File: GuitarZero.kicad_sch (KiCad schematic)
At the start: 9 parts, among them J2 USB_B_Micro, J3 AudioJack3_SwitchT, SW1 SW_Push, SW2 SW_Push, SW3 SW_Push, SW4 SW_Push, SW5 SW_Push, SW6 SW_Push

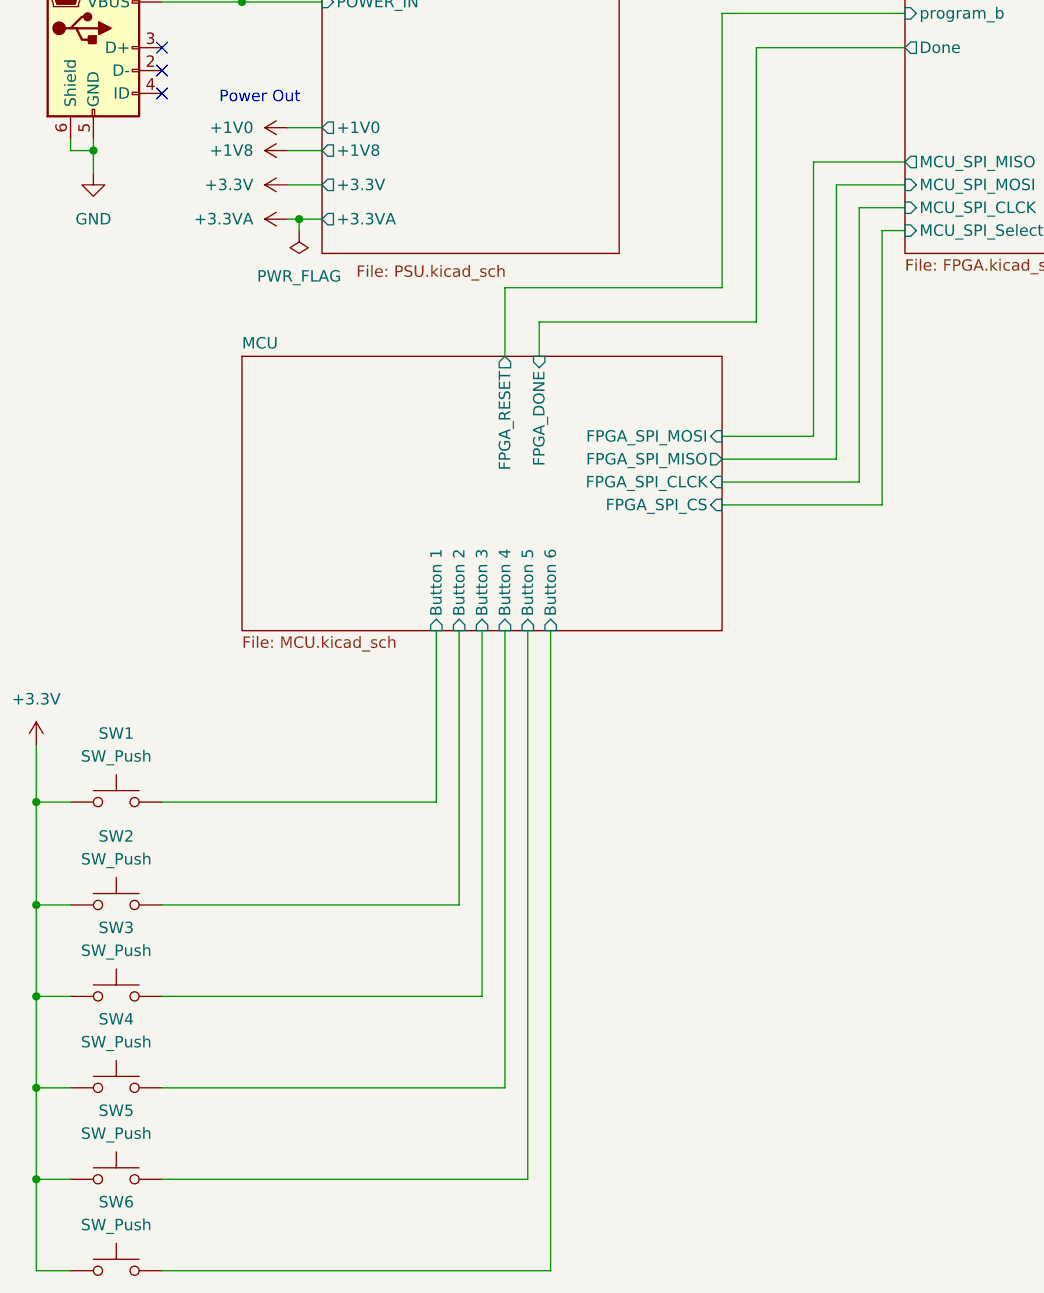
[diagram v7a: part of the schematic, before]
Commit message: Added labels in root for USB signals
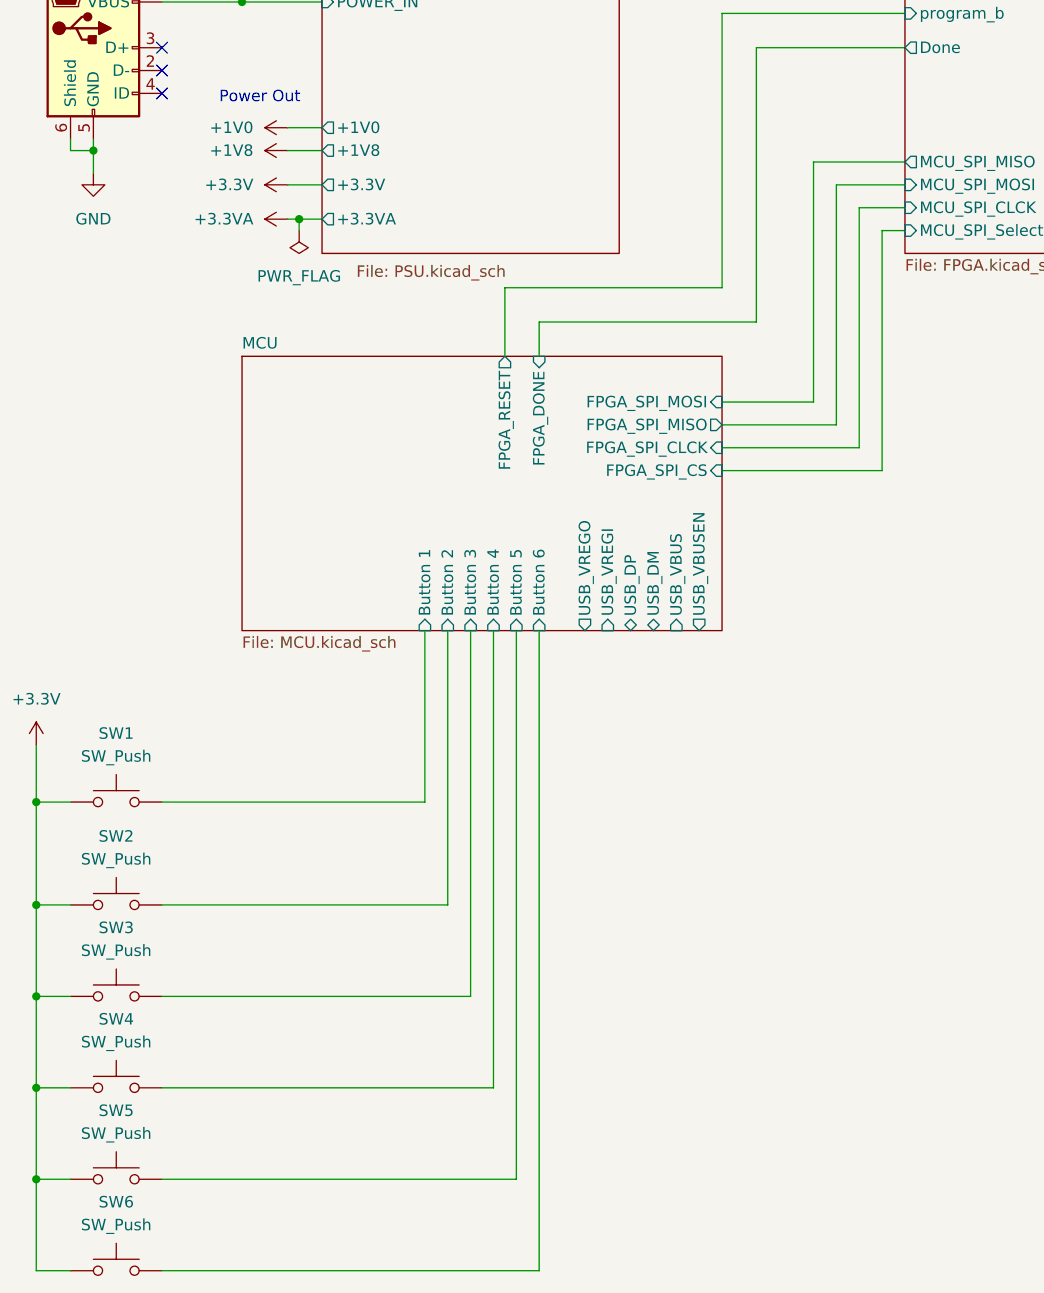
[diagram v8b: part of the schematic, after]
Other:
- sheet MCU ports: added USB_DM, USB_DP, USB_VBUS, USB_VBUSEN, USB_VREGI, USB_VREGO; removed none
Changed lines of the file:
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@@
   (no_connect (at 38.1 39.37))
   (no_connect (at 38.1 41.91))
-  (wire (pts (xy 38.1 162.56) (xy 78.74 162.56))
+  (wire (pts (xy 38.1 162.56) (xy 77.47 162.56))
     (stroke (width 0) (type default))
   )
@@
     (stroke (width 0) (type default))
   )
-  (wire (pts (xy 38.1 120.65) (xy 68.58 120.65))
+  (wire (pts (xy 38.1 120.65) (xy 67.31 120.65))
     (stroke (width 0) (type default))
   )
@@
     (stroke (width 0) (type default))
   )
-  (wire (pts (xy 73.66 142.24) (xy 73.66 101.6))
-    (stroke (width 0) (type default))
-  )
-  (wire (pts (xy 38.1 132.08) (xy 71.12 132.08))
-    (stroke (width 0) (type default))
-  )
-  (wire (pts (xy 38.1 152.4) (xy 76.2 152.4))
+  (wire (pts (xy 72.39 142.24) (xy 72.39 101.6))
+    (stroke (width 0) (type default))
+  )
+  (wire (pts (xy 38.1 132.08) (xy 69.85 132.08))
+    (stroke (width 0) (type default))
+  )
+  (wire (pts (xy 38.1 152.4) (xy 74.93 152.4))
     (stroke (width 0) (type default))
   )
@@
     (stroke (width 0) (type default))
   )
-  (wire (pts (xy 118.11 57.15) (xy 118.11 87.63))
+  (wire (pts (xy 118.11 57.15) (xy 118.11 83.82))
     (stroke (width 0) (type default))
   )
@@
     (stroke (width 0) (type default))
   )
-  (wire (pts (xy 76.2 152.4) (xy 76.2 101.6))
+  (wire (pts (xy 74.93 152.4) (xy 74.93 101.6))
     (stroke (width 0) (type default))
   )
@@
     (stroke (width 0) (type default))
   )
-  (wire (pts (xy 118.11 87.63) (xy 100.33 87.63))
+  (wire (pts (xy 118.11 83.82) (xy 100.33 83.82))
     (stroke (width 0) (type default))
   )
@@
     (stroke (width 0) (type default))
   )
-  (wire (pts (xy 115.57 54.61) (xy 115.57 85.09))
+  (wire (pts (xy 115.57 54.61) (xy 115.57 81.28))
     (stroke (width 0) (type default))
   )
@@
     (stroke (width 0) (type default))
   )
-  (wire (pts (xy 71.12 132.08) (xy 71.12 101.6))
+  (wire (pts (xy 69.85 132.08) (xy 69.85 101.6))
     (stroke (width 0) (type default))
   )
@@
     (stroke (width 0) (type default))
   )
-  (wire (pts (xy 78.74 162.56) (xy 78.74 101.6))
+  (wire (pts (xy 77.47 162.56) (xy 77.47 101.6))
     (stroke (width 0) (type default))
   )
@@
     (stroke (width 0) (type default))
   )
-  (wire (pts (xy 100.33 80.01) (xy 110.49 80.01))
+  (wire (pts (xy 100.33 76.2) (xy 110.49 76.2))
     (stroke (width 0) (type default))
   )
@@
     (stroke (width 0) (type default))
   )
-  (wire (pts (xy 38.1 172.72) (xy 81.28 172.72))
+  (wire (pts (xy 38.1 172.72) (xy 80.01 172.72))
     (stroke (width 0) (type default))
   )
@@
     (stroke (width 0) (type default))
   )
-  (wire (pts (xy 68.58 120.65) (xy 68.58 101.6))
+  (wire (pts (xy 67.31 120.65) (xy 67.31 101.6))
     (stroke (width 0) (type default))
   )
@@
     (stroke (width 0) (type default))
   )
-  (wire (pts (xy 110.49 80.01) (xy 110.49 49.53))
-    (stroke (width 0) (type default))
-  )
-  (wire (pts (xy 38.1 142.24) (xy 73.66 142.24))
-    (stroke (width 0) (type default))
-  )
-  (wire (pts (xy 113.03 82.55) (xy 113.03 52.07))
+  (wire (pts (xy 110.49 76.2) (xy 110.49 49.53))
+    (stroke (width 0) (type default))
+  )
+  (wire (pts (xy 38.1 142.24) (xy 72.39 142.24))
+    (stroke (width 0) (type default))
+  )
+  (wire (pts (xy 113.03 78.74) (xy 113.03 52.07))
     (stroke (width 0) (type default))
   )
@@
     (stroke (width 0) (type default))
   )
-  (wire (pts (xy 81.28 172.72) (xy 81.28 101.6))
+  (wire (pts (xy 80.01 172.72) (xy 80.01 101.6))
     (stroke (width 0) (type default))
   )
@@
     (stroke (width 0) (type default))
   )
-  (wire (pts (xy 100.33 82.55) (xy 113.03 82.55))
-    (stroke (width 0) (type default))
-  )
-  (wire (pts (xy 115.57 85.09) (xy 100.33 85.09))
+  (wire (pts (xy 100.33 78.74) (xy 113.03 78.74))
+    (stroke (width 0) (type default))
+  )
+  (wire (pts (xy 115.57 81.28) (xy 100.33 81.28))
     (stroke (width 0) (type default))
   )
@@
       (effects (font (size 1.27 1.27)) (justify left top))
     )
-    (pin "FPGA_SPI_MOSI" input (at 100.33 80.01 0)
+    (pin "FPGA_SPI_MOSI" input (at 100.33 76.2 0)
       (effects (font (size 1.27 1.27)) (justify right))
     )
-    (pin "FPGA_SPI_CS" input (at 100.33 87.63 0)
+    (pin "FPGA_SPI_CS" input (at 100.33 83.82 0)
       (effects (font (size 1.27 1.27)) (justify right))
     )
-    (pin "FPGA_SPI_CLCK" input (at 100.33 85.09 0)
+    (pin "FPGA_SPI_CLCK" input (at 100.33 81.28 0)
       (effects (font (size 1.27 1.27)) (justify right))
     )
-    (pin "FPGA_SPI_MISO" output (at 100.33 82.55 0)
+    (pin "FPGA_SPI_MISO" output (at 100.33 78.74 0)
       (effects (font (size 1.27 1.27)) (justify right))
     )
-    (pin "Button 6" input (at 81.28 101.6 270)
-      (effects (font (size 1.27 1.27)) (justify left))
-    )
-    (pin "Button 1" input (at 68.58 101.6 270)
-      (effects (font (size 1.27 1.27)) (justify left))
-    )
-    (pin "Button 2" input (at 71.12 101.6 270)
-      (effects (font (size 1.27 1.27)) (justify left))
-    )
-    (pin "Button 3" input (at 73.66 101.6 270)
-      (effects (font (size 1.27 1.27)) (justify left))
-    )
-    (pin "Button 4" input (at 76.2 101.6 270)
-      (effects (font (size 1.27 1.27)) (justify left))
-    )
-    (pin "Button 5" input (at 78.74 101.6 270)
+    (pin "Button 6" input (at 80.01 101.6 270)
+      (effects (font (size 1.27 1.27)) (justify left))
+    )
+    (pin "Button 1" input (at 67.31 101.6 270)
+      (effects (font (size 1.27 1.27)) (justify left))
+    )
+    (pin "Button 2" input (at 69.85 101.6 270)
+      (effects (font (size 1.27 1.27)) (justify left))
+    )
+    (pin "Button 3" input (at 72.39 101.6 270)
+      (effects (font (size 1.27 1.27)) (justify left))
+    )
+    (pin "Button 4" input (at 74.93 101.6 270)
+      (effects (font (size 1.27 1.27)) (justify left))
+    )
+    (pin "Button 5" input (at 77.47 101.6 270)
       (effects (font (size 1.27 1.27)) (justify left))
     )
@@
       (effects (font (size 1.27 1.27)) (justify right))
     )
-    (instances
+    (pin "USB_VREGO" output (at 85.09 101.6 270)
+      (effects (font (size 1.27 1.27)) (justify left))
+    )
+    (pin "USB_VREGI" input (at 87.63 101.6 270)
+      (effects (font (size 1.27 1.27)) (justify left))
+    )
+    (pin "USB_DP" bidirectional (at 90.17 101.6 270)
+      (effects (font (size 1.27 1.27)) (justify left))
+    )
+    (pin "USB_DM" bidirectional (at 92.71 101.6 270)
+      (effects (font (size 1.27 1.27)) (justify left))
+    )
+    (pin "USB_VBUS" input (at 95.25 101.6 270)
+      (effects (font (size 1.27 1.27)) (justify left))
+    )
+    (pin "USB_VBUSEN" output (at 97.79 101.6 270)
+      (effects (font (size 1.27 1.27)) (justify left))
+    )
+    (instances
